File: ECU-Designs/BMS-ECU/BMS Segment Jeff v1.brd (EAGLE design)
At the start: 110 x 132.8 mm, 90 parts, among them Q10 P-CHANNEL_MOSFET_DMP3099L-7, Q11 P-CHANNEL_MOSFET_DMP3099L-7, Q12 P-CHANNEL_MOSFET_DMP3099L-7, Q13 NPN_BCP56T1, Q3 P-CHANNEL_MOSFET_DMP3099L-7, Q4 P-CHANNEL_MOSFET_DMP3099L-7, Q5 P-CHANNEL_MOSFET_DMP3099L-7, Q6 P-CHANNEL_MOSFET_DMP3099L-7, Q8 P-CHANNEL_MOSFET_DMP3099L-7, Q9 P-CHANNEL_MOSFET_DMP3099L-7

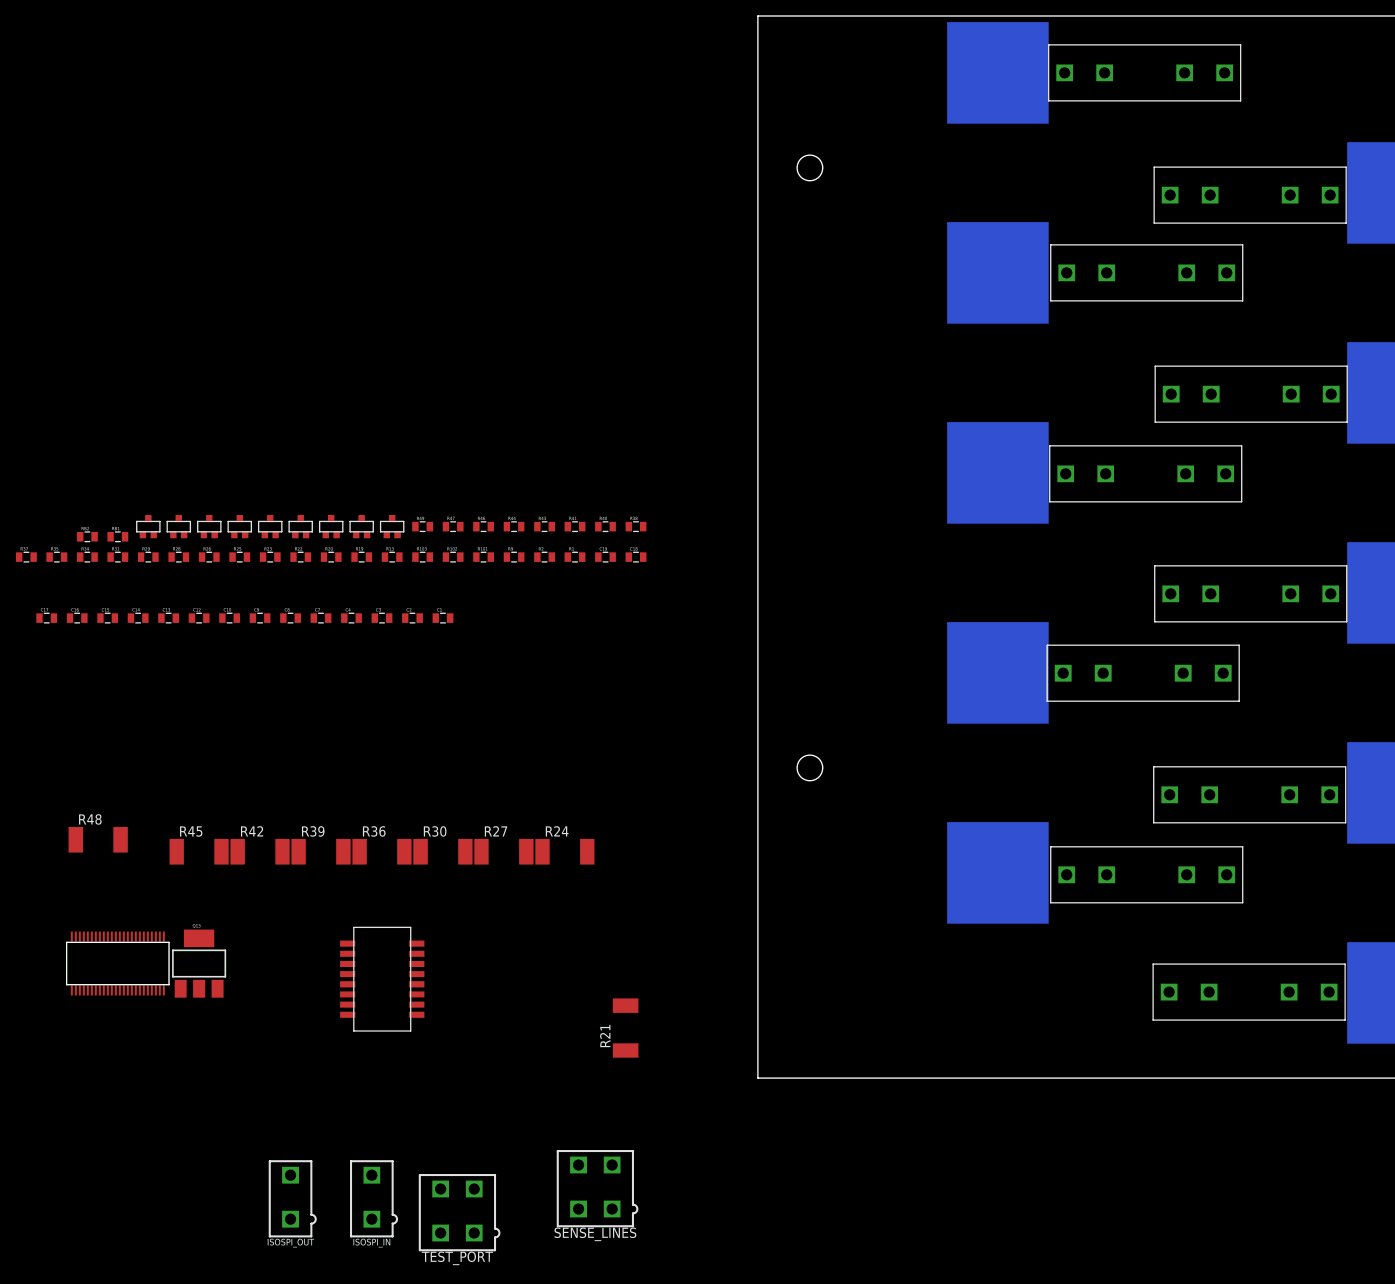
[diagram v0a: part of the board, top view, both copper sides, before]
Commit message: Renamed components in increasing order
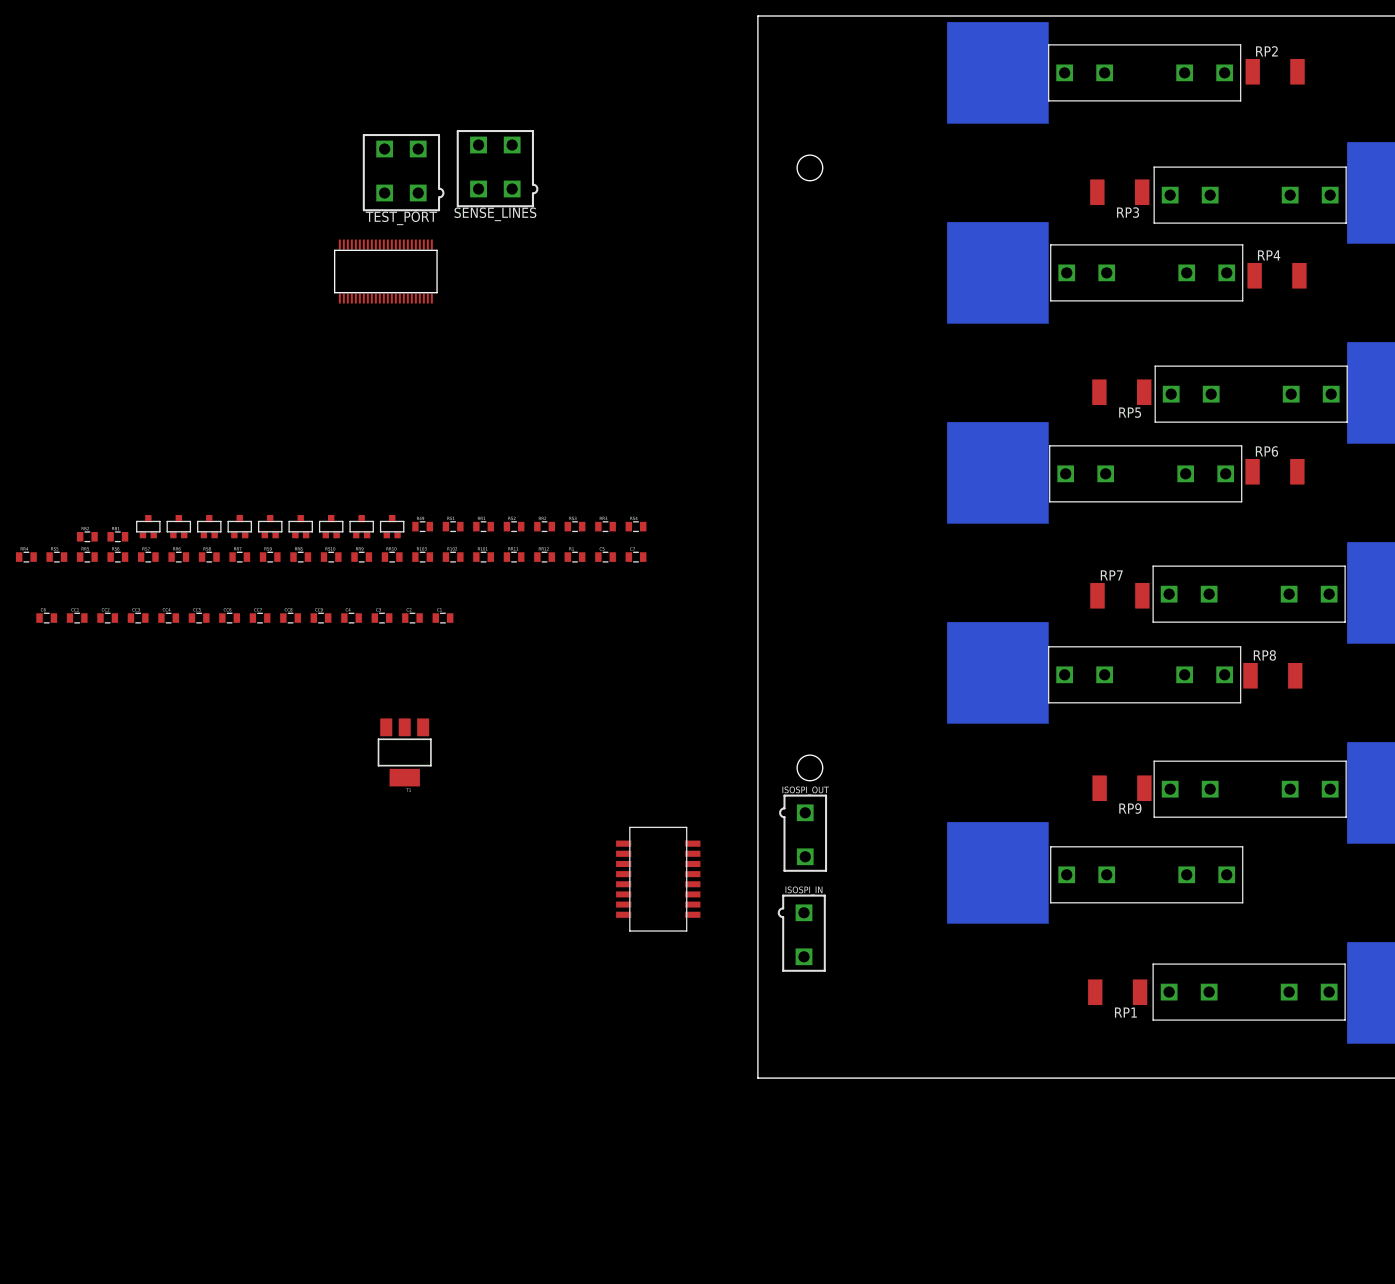
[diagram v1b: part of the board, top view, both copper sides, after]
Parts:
- removed C18: 100pF, HyTechDevices:0805
- removed Q13: NPN_BCP56T1, HyTechDevices:SOT223
- removed R21, R24, R27, R30, R36, R39, R42, R45, R48: 33Ω, HyTechDevices:R2512
- added CC9: 10nF, HyTechDevices:0805
- added RP1, RP2, RP3, RP4, RP5, RP6, RP7, RP8, RP9: 33Ω, HyTechDevices:R2512
- added T1: NPN_BCP56T1, HyTechDevices:SOT223
- C7: value 10nF -> 100pF
- moved TEST_PORT 130.2 mm to (-44.6, 134.6)
- moved SENSE_LINES 128.1 mm to (-32.8, 135.1)
- moved U$2 92.8 mm to (-46.5, 122.1)
- moved ISOSPI_OUT 78.7 mm to (5.92, 51.6), turned to 180 degrees
- moved ISOSPI_IN 63.2 mm to (5.76, 39.1), turned to 180 degrees
- moved C7 40.1 mm to (-15.2, 86.4)
- moved TRANSFORMER- 36.7 mm to (-12.5, 46.1)
- moved F2 0.70 mm to (61.5, 57.4), turned to 180 degrees
- moved F3 0.27 mm to (48.3, 71.7), turned to 0 degrees
- moved F4 0.20 mm to (61.4, 81.7), turned to 180 degrees
- renumbered C10 to CC6, C12 to CC5, C13 to CC4, C14 to CC3, C15 to CC2, C16 to CC1, C17 to C6, C19 to C5, C8 to CC8, C9 to CC7, Q10 to M3, Q11 to M2, Q12 to M1, Q3 to M9, Q4 to M8, Q5 to M7, Q6 to M6, Q8 to M5, Q9 to M4, R13 to RR10, R19 to RR9, R2 to RR12, R20 to RS10, R22 to RR8, R23 to RS9, R25 to RR7, R26 to RS8, R28 to RR6, R29 to RS7, R31 to RS6, R34 to RR5, R35 to RS5, R37 to RR4, R38 to RS4, R40 to RR3, R41 to RS3, R43 to RR2, R44 to RS2, R46 to RR1, R47 to RS1, R9 to RR11
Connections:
- net C10: now also CC9.1; no longer C7.1
- net C9: now also CC9.2; no longer C7.2
- net CELL2: now also RP9.1; no longer R21.1
- net CELL3: now also RP8.1; no longer R24.1
- net CELL4: now also RP7.1; no longer R27.1
- net CELL5: now also RP6.1; no longer R30.1
- net CELL6: now also RP5.1; no longer R36.1
- net CELL7: now also RP4.1; no longer R39.1
- net CELL8: now also RP3.1; no longer R42.1
- net CELL9: now also RP2.1; no longer R45.1
- net DRIVE: now also T1.1; no longer Q13.1
- net GND: now also C7.2, RP1.1; no longer C18.2, R48.1
- net N$1: now also C7.1; no longer C18.1
- net N$18: now also RP9.2; no longer R21.2
- net N$25: now also RP8.2; no longer R24.2
- net N$30: now also RP7.2; no longer R27.2
- net N$36: now also RP6.2; no longer R30.2
- net N$43: now also RP5.2; no longer R36.2
- net N$51: now also RP4.2; no longer R39.2
- net N$53: now also RP3.2; no longer R42.2
- net N$61: now also RP2.2; no longer R45.2
- net N$66: now also RP1.2; no longer R48.2
- net SUPPLY: now also T1.2, T1.4; no longer Q13.2, Q13.4
- net VREG: now also T1.3; no longer Q13.3

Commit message: Large changes to BMS schematic
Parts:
- removed CC1, CC2, CC3, CC4, CC5, CC6, CC7, CC8, CC9: 10nF, HyTechDevices:0805
- removed M1, M2, M3, M4, M5, M6, M7, M8, M9: P-CHANNEL_MOSFET_DMP3099L-7, HyTechDevices:SOT23
- removed RP1, RP2, RP3, RP4, RP5, RP6, RP7, RP8, RP9: 33Ω, HyTechDevices:R2512
- removed RR1, RR10, RR2, RR3, RR4, RR5, RR6, RR7, RR8, RR9, RS6: 100Ω, HyTechDevices:0805
- removed RS1, RS10, RS2, RS3, RS4, RS5, RS7, RS8, RS9: 3.3kΩ, HyTechDevices:0805
- added CELL9: (no value), HyTechDevices:KEYSTONE5222
- added CR0, CR1, CR2, CR3, CR4, CR5, CR6, CR7, CR8, CR9: 10nF, HyTechDevices:0805
- added DRAIN1:GATE1, DRAIN2:GATE1, DRAIN3:GATE1, DRAIN4:GATE1, DRAIN5:GATE1, DRAIN6:GATE1, DRAIN7:GATE1, DRAIN8:GATE1, DRAIN9:GATE1: 3.3kΩ, HyTechDevices:0805
- added DRAIN1:PFET1, DRAIN2:PFET1, DRAIN3:PFET1, DRAIN4:PFET1, DRAIN5:PFET1, DRAIN6:PFET1, DRAIN7:PFET1, DRAIN8:PFET1, DRAIN9:PFET1: P-CHANNEL_MOSFET_DMP3099L-7, HyTechDevices:SOT23
- added DRAIN1:W1, DRAIN2:W1, DRAIN3:W1, DRAIN4:W1, DRAIN5:W1, DRAIN6:W1, DRAIN7:W1, DRAIN8:W1, DRAIN9:W1: 33Ω, HyTechDevices:R2512
- added GLV_CONTROL: CPC1002N, HyTechDevices:SOP04
- added RC0, RC1, RC10, RC2, RC3, RC4, RC5, RC6, RC7, RC8, RC9: 100Ω, HyTechDevices:0805
- added X1: MINIFIT_5566-2, HyTechDevices:MINIFIT_5566-2
- G1: value (none) -> 100Ω; device HyTechDevices:KEYSTONE5222 -> HyTechDevices:0805
- TEST_PORT: value MINIFIT_5566-4 -> (none)
- moved G1 339.8 mm to (-309.0, 23.5), flipped to the top
- moved U$2 156.0 mm to (100.6, 70.0), turned to 270 degrees
- moved C3 151.1 mm to (102.5, 56.8), flipped to the bottom, turned to 180 degrees
- moved C2 147.8 mm to (102.6, 54.0), flipped to the bottom, turned to 180 degrees
- moved C1 144.6 mm to (102.6, 51.3), flipped to the bottom, turned to 180 degrees
- moved F1 100.2 mm to (48.3, 146.9)
- moved F9 100.2 mm to (48.6, 46.6)
- moved F2 74.3 mm to (61.5, 131.6)
- moved F8 74.3 mm to (61.5, 57.4)
- moved F3 50.2 mm to (48.6, 121.9)
- moved F7 50.2 mm to (48.3, 71.7)
- moved F4 25.0 mm to (61.7, 106.7)
- moved F6 25.0 mm to (61.4, 81.7)
- moved C6 6.00 mm to (-82.9, 78.7)
- renumbered C4 to SC1, C5 to SC2, G0 to CELL0, G2 to CELL8, G3 to CELL7, G4 to CELL6, G5 to CELL5, G6 to CELL4, G7 to CELL3, G8 to CELL2, G9 to CELL1, RR11 to S2, RR12 to S1
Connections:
- net G0 renamed CC0
- net G5 renamed CC5
- removed net CELL1: F1.R1, F1.R2, M9.2, RR10.1, RR9.1, S1.1, S2.1, TEST_PORT.1
- removed net CELL2: F2.R1, F2.R2, M8.2, RP9.1, RR8.1, TEST_PORT.2, TEST_PORT.3
- removed net CELL3: F3.R1, F3.R2, M7.2, RP8.1, RR7.1, TEST_PORT.4
- removed net CELL4: F4.R1, F4.R2, M6.2, RP7.1, RR6.1
- removed net CELL5: F5.R1, F5.R2, M5.2, RP6.1, RR5.1, RS6.1
- removed net CELL6: F6.R1, F6.R2, M4.2, RP5.1, RR4.1
- removed net CELL7: F7.R1, F7.R2, M3.2, RP4.1, RR3.1
- removed net CELL8: F8.R1, F8.R2, M2.2, RP3.1, RR2.1
- removed net CELL9: F9.R1, F9.R2, M1.2, RP2.1, RR1.1
- removed net G1: F1.L1, F1.L2, G1.P$1
- removed net G2: CELL8.P$1, F2.L1, F2.L2
- removed net G3: CELL7.P$1, F3.L1, F3.L2
- removed net G4: CELL6.P$1, F4.L1, F4.L2
- removed net G6: CELL4.P$1, F6.L1, F6.L2
- removed net G7: CELL3.P$1, F7.L1, F7.L2
- removed net G8: CELL2.P$1, F8.L1, F8.L2
- removed net G9: CELL1.P$1, F9.L1, F9.L2
- removed net N$15: M9.1, RS10.1
- removed net N$18: M9.3, RP9.2
- removed net N$20: M5.1, RS5.1
- removed net N$22: M4.1, RS4.1
- removed net N$25: M8.3, RP8.2
- removed net N$27: M3.1, RS3.1
- removed net N$28: M2.1, RS2.1
- removed net N$29: M1.1, RS1.1
- removed net N$30: M7.3, RP7.2
- removed net N$36: M6.3, RP6.2
- removed net N$43: M5.3, RP5.2
- removed net N$51: M4.3, RP4.2
- removed net N$53: M3.3, RP3.2
- removed net N$61: M2.3, RP2.2
- removed net N$66: M1.3, RP1.2
- removed net N$68: M8.1, RS9.1
- removed net N$69: M7.1, RS8.1
- removed net N$70: M6.1, RS7.1
- removed net UNUSED_CELL_LINES_1: RR10.2, U$2.2, U$2.4
- removed net UNUSED_CELL_LINES_2: RS6.2, U$2.14
- new net C0: CR0.1, CR1.2, RC0.2, U$2.26
- new net C11: U$2.4
- new net C12: U$2.2
- new net C6: CR6.1, CR7.2, RC6.2, U$2.14
- new net CC1: CELL1.P$1, F1.L1, F1.L2
- new net CC2: CELL2.P$1, F2.L1, F2.L2
- new net CC3: CELL3.P$1, F3.L1, F3.L2
- new net CC4: CELL4.P$1, F4.L1, F4.L2
- new net CC6: CELL6.P$1, F6.L1, F6.L2
- new net CC7: CELL7.P$1, F7.L1, F7.L2
- new net CC8: CELL8.P$1, F8.L1, F8.L2
- new net CC9: CELL9.P$1, F9.L1, F9.L2
- new net DRAIN1:DRAIN: DRAIN1:PFET1.3, DRAIN1:W1.2
- new net DRAIN1:GATE: DRAIN1:GATE1.1, DRAIN1:PFET1.1
- new net DRAIN2:DRAIN: DRAIN2:PFET1.3, DRAIN2:W1.2
- new net DRAIN2:GATE: DRAIN2:GATE1.1, DRAIN2:PFET1.1
- new net DRAIN3:DRAIN: DRAIN3:PFET1.3, DRAIN3:W1.2
- new net DRAIN3:GATE: DRAIN3:GATE1.1, DRAIN3:PFET1.1
- new net DRAIN4:DRAIN: DRAIN4:PFET1.3, DRAIN4:W1.2
- new net DRAIN4:GATE: DRAIN4:GATE1.1, DRAIN4:PFET1.1
- new net DRAIN5:DRAIN: DRAIN5:PFET1.3, DRAIN5:W1.2
- new net DRAIN5:GATE: DRAIN5:GATE1.1, DRAIN5:PFET1.1
- new net DRAIN6:DRAIN: DRAIN6:PFET1.3, DRAIN6:W1.2
- new net DRAIN6:GATE: DRAIN6:GATE1.1, DRAIN6:PFET1.1
- new net DRAIN7:DRAIN: DRAIN7:PFET1.3, DRAIN7:W1.2
- new net DRAIN7:GATE: DRAIN7:GATE1.1, DRAIN7:PFET1.1
- new net DRAIN8:DRAIN: DRAIN8:PFET1.3, DRAIN8:W1.2
- new net DRAIN8:GATE: DRAIN8:GATE1.1, DRAIN8:PFET1.1
- new net DRAIN9:DRAIN: DRAIN9:PFET1.3, DRAIN9:W1.2
- new net DRAIN9:GATE: DRAIN9:GATE1.1, DRAIN9:PFET1.1
- new net N$10: G1.1, GLV_CONTROL.2
- new net N$11: GLV_CONTROL.1, X1.1
- new net N$3: GLV_CONTROL.3, S1.1, S2.1
- new net S11: U$2.5
- new net S12: U$2.3
- new net S6: DRAIN6:GATE1.2, U$2.15
- new net SENSE1: F1.R1, F1.R2, TEST_PORT.2
- new net SENSE1_J: DRAIN1:PFET1.2, DRAIN2:W1.1, RC1.1, TEST_PORT.4
- new net SENSE2: DRAIN2:PFET1.2, DRAIN3:W1.1, F2.R1, F2.R2, RC2.1
- new net SENSE3: DRAIN3:PFET1.2, DRAIN4:W1.1, F3.R1, F3.R2, RC3.1
- new net SENSE4: DRAIN4:PFET1.2, DRAIN5:W1.1, F4.R1, F4.R2, RC4.1
- new net SENSE5: DRAIN5:PFET1.2, DRAIN6:W1.1, F5.R1, F5.R2, RC5.1
- new net SENSE6: DRAIN6:PFET1.2, DRAIN7:W1.1, F6.R1, F6.R2, RC6.1
- new net SENSE7: DRAIN7:PFET1.2, DRAIN8:W1.1, F7.R1, F7.R2, RC7.1
- new net SENSE8: DRAIN8:PFET1.2, DRAIN9:W1.1, F8.R1, F8.R2, RC8.1
- new net SENSE9: DRAIN9:PFET1.2, F9.R1, F9.R2, GLV_CONTROL.4, RC10.1, RC9.1
- new net V-: C1.2, C2.2, C3.2, C6.2, C7.2, CR0.2, DRAIN1:W1.1, F0.R1, F0.R2, RB2.1, RC0.1, SC1.2, SC2.2, TEST_PORT.3, U$2.30, U$2.31, U$2.43, U$2.44
- net C1: now also CR1.1, CR2.2, RC1.2; no longer CC1.1, CC2.2, RR1.2
- net C10: now also RC10.2; no longer CC9.1, RR9.2
- net C2: now also CR2.1, CR3.2, RC2.2; no longer CC2.1, CC3.2, RR2.2
- net C3: now also CR3.1, CR4.2, RC3.2; no longer CC3.1, CC4.2, RR3.2
- net C4: now also CR4.1, CR5.2, RC4.2; no longer CC4.1, CC5.2, RR4.2
- net C5: now also CR5.1, CR6.2, RC5.2; no longer CC5.1, CC6.2, RR5.2
- net C7: now also CR7.1, CR8.2, RC7.2; no longer CC6.1, CC7.2, RR6.2
- net C8: now also CR8.1, CR9.2, RC8.2; no longer CC7.1, CC8.2, RR7.2
- net C9: now also CR9.1, RC9.2; no longer CC8.1, CC9.2, RR8.2
- net GND: now also G1.2, X1.2; no longer C1.2, C2.2, C3.2, C6.2, C7.2, CC1.2, F0.R1, F0.R2, RB2.1, RP1.1, SC1.2, SC2.2, U$2.26, U$2.30, U$2.31, U$2.43, U$2.44
- net S1: now also DRAIN1:GATE1.2; no longer RS1.2
- net S10: no longer RS10.2
- net S2: now also DRAIN2:GATE1.2; no longer RS2.2
- net S3: now also DRAIN3:GATE1.2; no longer RS3.2
- net S4: now also DRAIN4:GATE1.2; no longer RS4.2
- net S5: now also DRAIN5:GATE1.2; no longer RS5.2
- net S7: now also DRAIN7:GATE1.2; no longer RS7.2
- net S8: now also DRAIN8:GATE1.2; no longer RS8.2
- net S9: now also DRAIN9:GATE1.2; no longer RS9.2
- net SUPPLY: now also SC1.1; no longer SC2.1
- net V+: now also SC2.1; no longer SC1.1

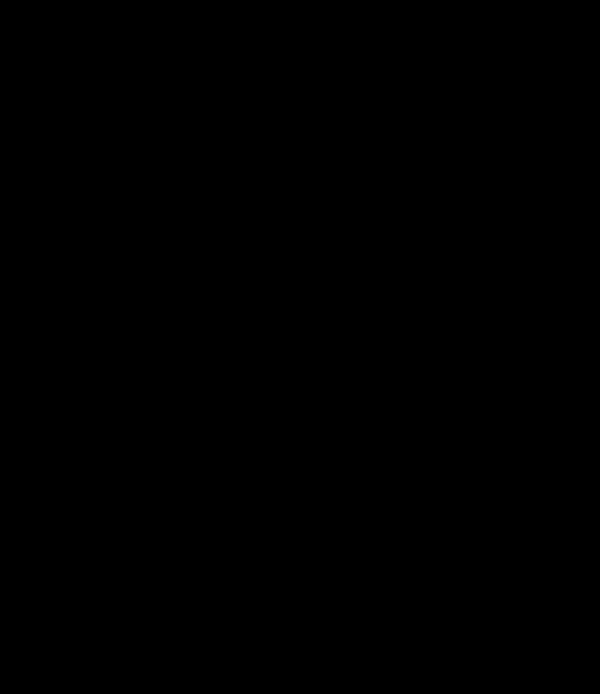
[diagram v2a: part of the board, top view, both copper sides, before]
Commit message: Small detailed changes to BMS (negative) schematic
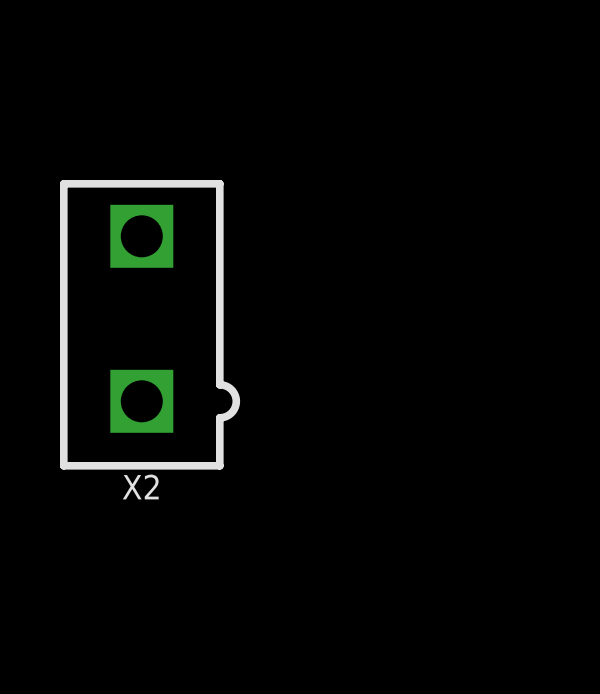
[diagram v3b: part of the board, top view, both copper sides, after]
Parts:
- added X2: To Positive BMS, HyTechDevices:MINIFIT_5566-2
- RB1, RB2: value (none) -> 1.2k
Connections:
- net CC9: now also X2.1, X2.2
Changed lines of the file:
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@@
 <element name="R49" library="HyTechDevices" package="0805" value="120Ω" x="-41.91" y="90.17"/>
 <element name="S2" library="HyTechDevices" package="0805" value="100Ω" x="-30.48" y="86.36"/>
-<element name="RB1" library="HyTechDevices" package="0805" value="" x="-80.01" y="88.9"/>
-<element name="RB2" library="HyTechDevices" package="0805" value="" x="-83.82" y="88.9"/>
+<element name="RB1" library="HyTechDevices" package="0805" value="1.2k" x="-80.01" y="88.9"/>
+<element name="RB2" library="HyTechDevices" package="0805" value="1.2k" x="-83.82" y="88.9"/>
 <element name="SENSE_LINES" library="HyTechDevices" package="MINIFIT_5566-4" value="MINIFIT_5566-4" x="-32.82" y="135.12">
 <attribute name="MF" value="" x="-32.82" y="135.12" size="1.778" layer="27" display="off"/>
@@
 <attribute name="OC_NEWARK" value="unknown" x="-321.5" y="34.5" size="1.778" layer="27" display="off"/>
 </element>
+<element name="X2" library="HyTechDevices" package="MINIFIT_5566-2" value="To Positive BMS" x="-342.5" y="34.5">
+<attribute name="MF" value="" x="-342.5" y="34.5" size="1.778" layer="27" display="off"/>
+<attribute name="MPN" value="" x="-342.5" y="34.5" size="1.778" layer="27" display="off"/>
+<attribute name="OC_FARNELL" value="1822072" x="-342.5" y="34.5" size="1.778" layer="27" display="off"/>
+<attribute name="OC_NEWARK" value="unknown" x="-342.5" y="34.5" size="1.778" layer="27" display="off"/>
+</element>
 </elements>
 <signals>
@@
 <contactref element="F9" pad="L2"/>
 <contactref element="CELL9" pad="P$1"/>
+<contactref element="X2" pad="1"/>
+<contactref element="X2" pad="2"/>
 <wire x1="38.6" y1="46.65" x2="43.6" y2="46.65" width="0" layer="19" extent="1-1"/>
 <wire x1="30" y1="46.889" x2="38.6" y2="46.65" width="0" layer="19" extent="16-16"/>
+<wire x1="-342.5" y1="37.25" x2="30" y2="46.889" width="0" layer="19" extent="16-16"/>
+<wire x1="-342.5" y1="31.75" x2="-342.5" y2="37.25" width="0" layer="19" extent="1-1"/>
 </signal>
 <signal name="CC8">
@@
 <contactref element="C2" pad="2"/>
 <contactref element="C1" pad="2"/>
-<contactref element="U$2" pad="31"/>
-<contactref element="U$2" pad="30"/>
 <contactref element="F0" pad="R1"/>
 <contactref element="F0" pad="R2"/>
@@
 <contactref element="U$2" pad="43"/>
 <contactref element="RB2" pad="1"/>
+<contactref element="U$2" pad="31"/>
+<contactref element="U$2" pad="30"/>
 <wire x1="103.935" y1="73.26" x2="103.935" y2="73.76" width="0" layer="19" extent="1-1"/>
 <wire x1="103.935" y1="67.26" x2="103.935" y2="73.26" width="0" layer="19" extent="1-1"/>

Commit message: Mega BMS Progress (Negative side board layout)
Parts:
- C6, C7: value 100pF -> 25pF
- moved CR9 390.1 mm to (77.6, 142.0), turned to 270 degrees
- moved RC10 386.3 mm to (69.1, 146.8)
- moved RC9 379.4 mm to (69.1, 143.0)
- moved CR8 366.7 mm to (81.0, 121.0), turned to 270 degrees
- moved X2 364.8 mm to (5.00, 145.5)
- moved RC8 359.9 mm to (76.5, 122.5)
- moved DRAIN9:GATE1 347.6 mm to (52.5, 138.5)
- moved DRAIN9:PFET1 346.0 mm to (47.0, 140.0), turned to 90 degrees
- moved DRAIN9:W1 344.2 mm to (41.5, 134.5), turned to 90 degrees
- moved DRAIN8:GATE1 344.0 mm to (76.5, 119.0)
- moved DRAIN8:PFET1 343.0 mm to (71.5, 121.0), turned to 90 degrees
- moved DRAIN8:W1 342.2 mm to (65.0, 121.0)
- moved X1 338.9 mm to (4.50, 127.0), turned to 180 degrees
- moved G1 334.2 mm to (10.0, 123.0), turned to 180 degrees
- moved GLV_CONTROL 333.2 mm to (14.0, 129.0), turned to 270 degrees
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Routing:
- net V-: track 0.00 -> 67.2 mm, vias 0 -> 3
- net SENSE1: track 0.00 -> 48.7 mm
- net SENSE8: track 0.00 -> 43.6 mm, vias 0 -> 2
- net SENSE6: track 0.00 -> 42.8 mm, vias 0 -> 2
- net SENSE4: track 0.00 -> 41.9 mm, vias 0 -> 2
- net SENSE2: track 0.00 -> 41.8 mm, vias 0 -> 2
- net DRAIN2:DRAIN: track 0.00 -> 35.8 mm, vias 0 -> 2
- net SENSE9: track 0.00 -> 29.2 mm, vias 0 -> 2
- net C2: track 0.00 -> 25.3 mm
- net SENSE1_J: track 0.00 -> 24.7 mm, vias 0 -> 1
- net C4: track 0.00 -> 23.5 mm
- net C8: track 0.00 -> 22.6 mm
- net SENSE3: track 0.00 -> 22.5 mm, vias 0 -> 1
- net C3: track 0.00 -> 22.3 mm
- net SENSE5: track 0.00 -> 21.9 mm, vias 0 -> 1
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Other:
- board size 110 x 132.8 mm -> 110 x 130.8 mm
